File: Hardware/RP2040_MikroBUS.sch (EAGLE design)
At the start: 74 parts, among them J1 SWD, J3 Qwiic, J5 USB C, J6 microSD, Q1 20V/4.2A/52mΩ/1.4W, U2 MAX17048, U3 MCP73831, U4 W25QXX128MBIT, U5 RP2040, U6 WS2812-2020, U7 3.3V, Y2 12MHz

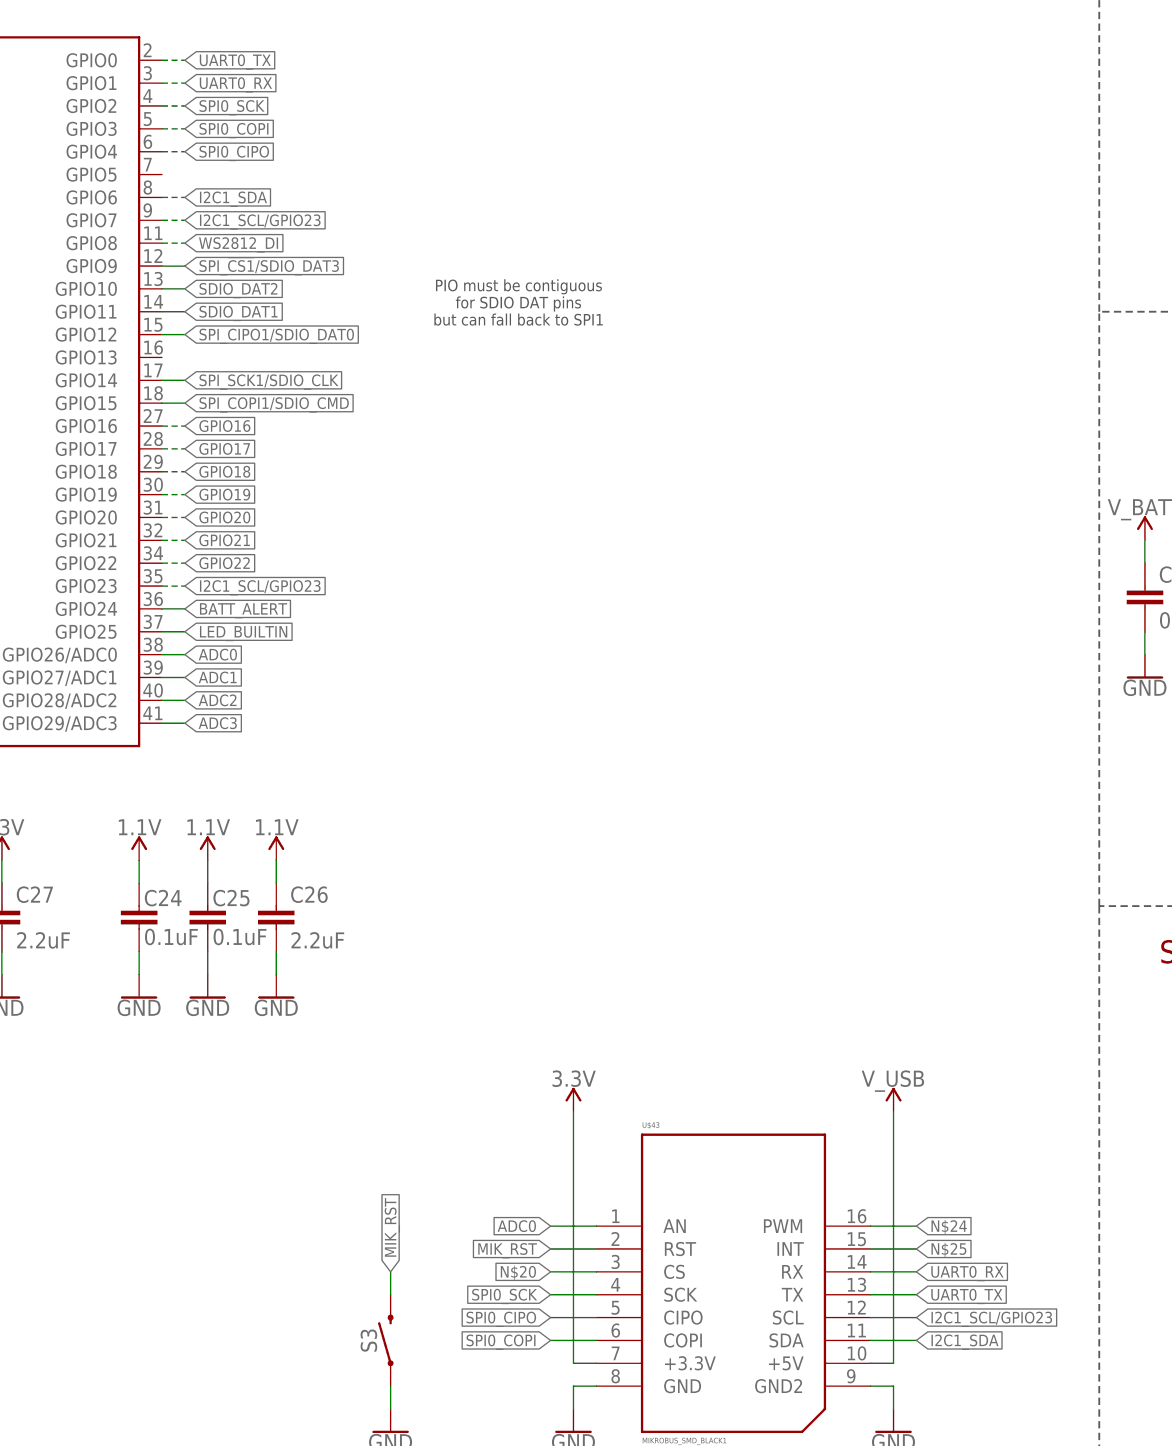
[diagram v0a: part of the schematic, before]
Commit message: Rename eagle files
Make sure everything is connected in the schematic
Parts are laid out where they should be on board, need to just route/re-route.
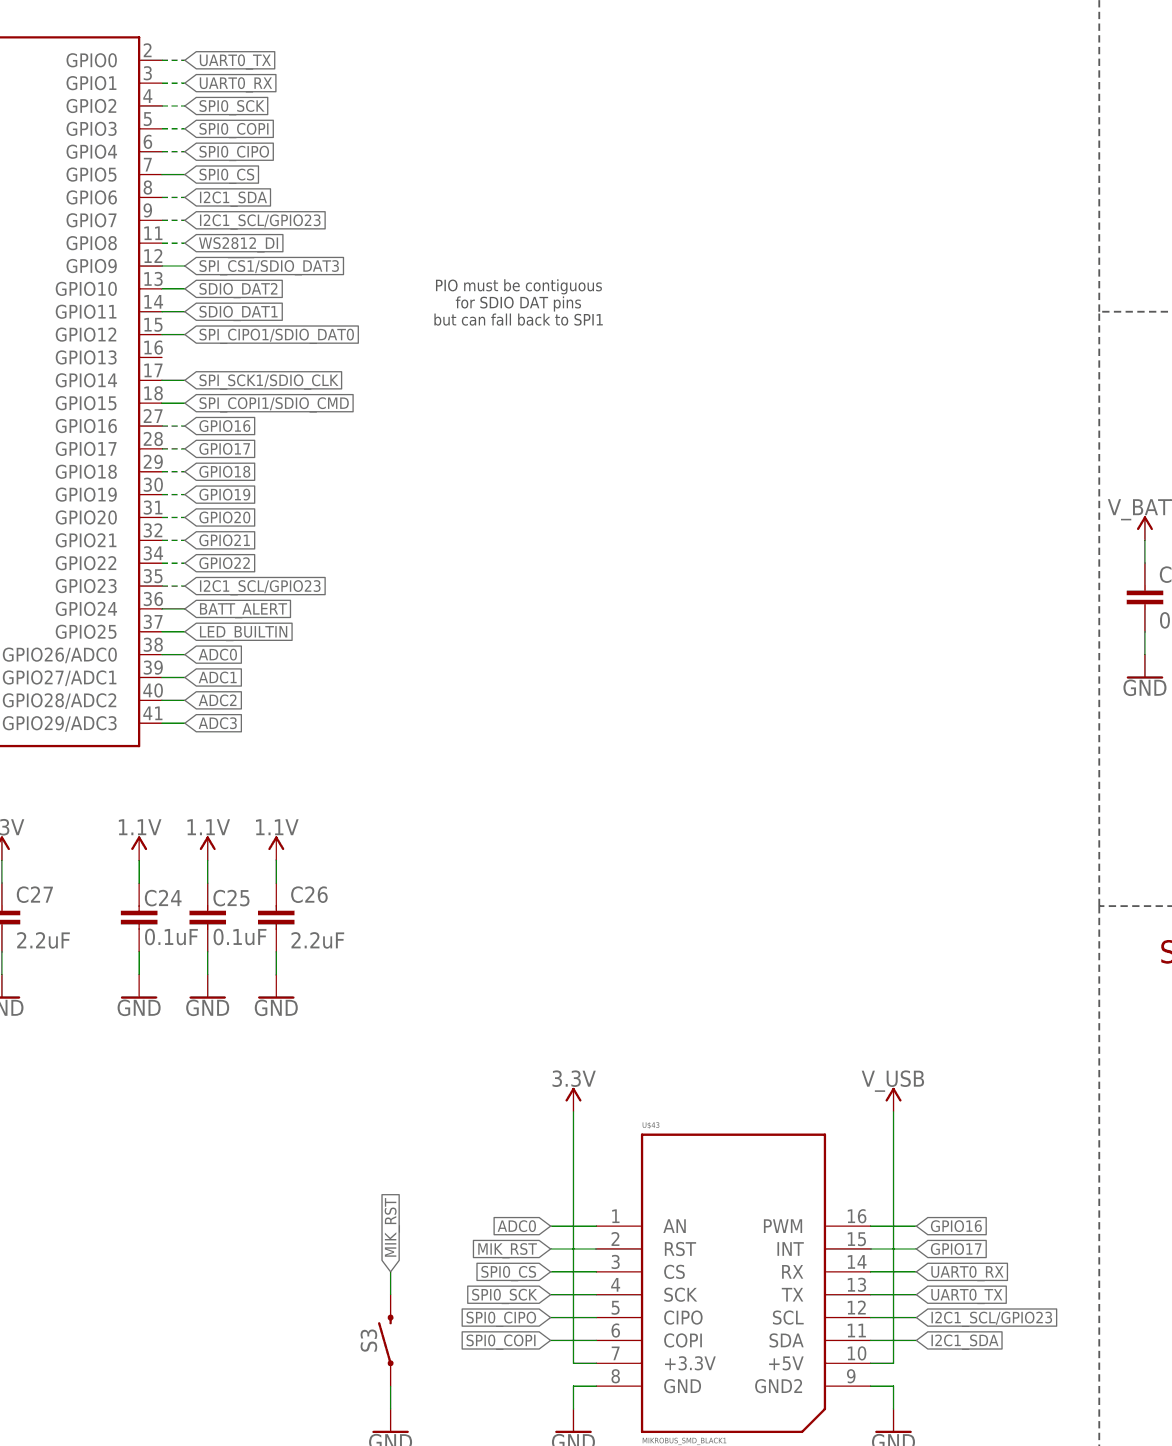
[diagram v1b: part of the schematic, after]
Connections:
- removed net N$20: U$43.CS
- removed net N$24: U$43.PWM
- removed net N$25: U$43.INT
- new net SPI0_CS: U$43.CS, U5.GPIO5
- net GPIO16: now also U$43.PWM
- net GPIO17: now also U$43.INT
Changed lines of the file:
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@@
 <?xml version="1.0" encoding="utf-8"?>
 <!DOCTYPE eagle SYSTEM "eagle.dtd">
-<eagle version="9.4.2">
+<eagle version="9.5.2">
 <drawing>
 <settings>
-<setting alwaysvectorfont="yes"/>
+<setting alwaysvectorfont="no"/>
 <setting keepoldvectorfont="yes"/>
 <setting verticaltext="up"/>
@@
 <label x="365.76" y="81.28" size="1.27" layer="95" rot="R180" xref="yes"/>
 </segment>
+<segment>
+<pinref part="U$43" gate="J1" pin="PWM"/>
+<wire x1="172.72" y1="30.48" x2="177.8" y2="30.48" width="0.1524" layer="91"/>
+<label x="177.8" y="30.48" size="1.27" layer="95" xref="yes"/>
+</segment>
 </net>
 <net name="GPIO17" class="0">
@@
 <wire x1="368.3" y1="78.74" x2="365.76" y2="78.74" width="0.1524" layer="91" style="longdash"/>
 <label x="365.76" y="78.74" size="1.27" layer="95" rot="R180" xref="yes"/>
+</segment>
+<segment>
+<pinref part="U$43" gate="J1" pin="INT"/>
+<wire x1="172.72" y1="27.94" x2="177.8" y2="27.94" width="0.1524" layer="91"/>
+<label x="177.8" y="27.94" size="1.27" layer="95" xref="yes"/>
 </segment>
 </net>
@@
 </segment>
 </net>
-<net name="N$20" class="0">
+<net name="SPI0_CS" class="0">
+<segment>
+<pinref part="U5" gate="U1" pin="GPIO5"/>
+<wire x1="93.98" y1="147.32" x2="96.52" y2="147.32" width="0.1524" layer="91"/>
+<label x="96.52" y="147.32" size="1.27" layer="95" xref="yes"/>
+</segment>
 <segment>
 <pinref part="U$43" gate="J1" pin="CS"/>
@@
 </segment>
 </net>
-<net name="N$24" class="0">
-<segment>
-<pinref part="U$43" gate="J1" pin="PWM"/>
-<wire x1="172.72" y1="30.48" x2="177.8" y2="30.48" width="0.1524" layer="91"/>
-<label x="177.8" y="30.48" size="1.27" layer="95" xref="yes"/>
-</segment>
-</net>
-<net name="N$25" class="0">
-<segment>
-<pinref part="U$43" gate="J1" pin="INT"/>
-<wire x1="172.72" y1="27.94" x2="177.8" y2="27.94" width="0.1524" layer="91"/>
-<label x="177.8" y="27.94" size="1.27" layer="95" xref="yes"/>
-</segment>
-</net>

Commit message: Routing finished!
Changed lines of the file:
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@@
 <?xml version="1.0" encoding="utf-8"?>
 <!DOCTYPE eagle SYSTEM "eagle.dtd">
-<eagle version="9.5.2">
+<eagle version="9.4.2">
 <drawing>
 <settings>
-<setting alwaysvectorfont="no"/>
+<setting alwaysvectorfont="yes"/>
 <setting keepoldvectorfont="yes"/>
 <setting verticaltext="up"/>
@@
 <layer number="56" name="wert" color="7" fill="1" visible="no" active="no"/>
 <layer number="57" name="tCAD" color="7" fill="1" visible="no" active="no"/>
+<layer number="58" name="bCopper" color="7" fill="1" visible="no" active="no"/>
 <layer number="59" name="tCarbon" color="7" fill="1" visible="no" active="no"/>
 <layer number="60" name="bCarbon" color="7" fill="1" visible="no" active="no"/>
@@
 <layer number="154" name="FabDoc2" color="7" fill="1" visible="yes" active="yes"/>
 <layer number="155" name="FabDoc3" color="7" fill="1" visible="yes" active="yes"/>
+<layer number="156" name="gesam-Maß" color="1" fill="7" visible="no" active="no"/>
+<layer number="157" name="FaceMchng" color="3" fill="1" visible="no" active="no"/>
+<layer number="158" name="FaceMMeas" color="3" fill="1" visible="no" active="no"/>
+<layer number="159" name="Geh-Bear2" color="1" fill="7" visible="no" active="no"/>
+<layer number="160" name="Topologie" color="9" fill="1" visible="no" active="no"/>
+<layer number="161" name="tomplace2" color="7" fill="1" visible="no" active="no"/>
 <layer number="166" name="AntennaArea" color="7" fill="1" visible="no" active="no"/>
 <layer number="168" name="4mmHeightArea" color="7" fill="1" visible="no" active="no"/>
@@
 <layer number="250" name="Descript" color="3" fill="1" visible="no" active="no"/>
 <layer number="251" name="SMDround" color="12" fill="11" visible="no" active="no"/>
+<layer number="252" name="BR-BS" color="7" fill="1" visible="no" active="no"/>
+<layer number="253" name="Extra" color="7" fill="1" visible="no" active="no"/>
 <layer number="254" name="cooling" color="7" fill="1" visible="yes" active="yes"/>
 <layer number="255" name="routoute" color="7" fill="1" visible="yes" active="yes"/>
@@
 <part name="SUPPLY36" library="SparkFun-PowerSymbols" deviceset="3.3V" device=""/>
 <part name="GND42" library="SparkFun-PowerSymbols" deviceset="GND" device=""/>
-<part name="TP1" library="SparkFun-Connectors" deviceset="TEST-POINT" device="3X4" value=""/>
-<part name="TP2" library="SparkFun-Connectors" deviceset="TEST-POINT" device="3X4" value=""/>
-<part name="TP3" library="SparkFun-Connectors" deviceset="TEST-POINT" device="3X4" value=""/>
+<part name="TP1" library="SparkFun-Connectors" deviceset="TEST-POINT" device="3X4" value="TEST-POINT3X4"/>
+<part name="TP2" library="SparkFun-Connectors" deviceset="TEST-POINT" device="3X4" value="TEST-POINT3X4"/>
+<part name="TP3" library="SparkFun-Connectors" deviceset="TEST-POINT" device="3X4" value="TEST-POINT3X4"/>
 <part name="U$43" library="mikroBUS_SMD_BLACK" deviceset="MIKROBUS_SMD_BLACK" device="1" package3d_urn="urn:adsk.eagle:package:18494266/4"/>
 <part name="GND43" library="SparkFun-PowerSymbols" deviceset="GND" device=""/>

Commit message: Made board dimensions on grid
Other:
- note added: "MikroBUS socket"
- note added: "v01"
- note removed: "v10"
- moved on the sheet: C17, C18, C20, C21, C22, C23, C24, C25, C26, C27

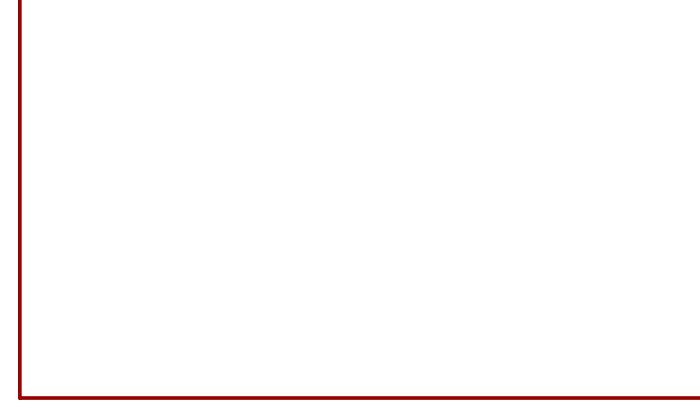
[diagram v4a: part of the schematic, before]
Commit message: More of Pete's updates
* Fix I2C jumper label
* Update RP2040 logo and add to SF Eagle libraries
* Change "Mik" to "Mikro" for mikroBUS reset button
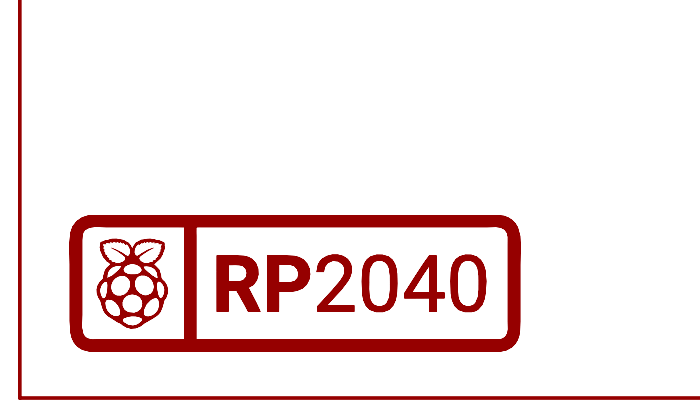
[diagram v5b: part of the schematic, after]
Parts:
- added U$17, U$73: RASPI_RP2040_LOGO_10MM, SparkFun-Aesthetics:RASPI_RP2040_LOGO_10MM
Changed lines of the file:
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@@
 <?xml version="1.0" encoding="utf-8"?>
 <!DOCTYPE eagle SYSTEM "eagle.dtd">
-<eagle version="9.5.2">
+<eagle version="9.4.2">
 <drawing>
 <settings>
-<setting alwaysvectorfont="no"/>
+<setting alwaysvectorfont="yes"/>
 <setting keepoldvectorfont="yes"/>
 <setting verticaltext="up"/>
@@
 <part name="S3" library="SparkFun-Switches" deviceset="MOMENTARY-SWITCH-SPST" device="-SMD-5.2MM-TALL"/>
 <part name="GND45" library="SparkFun-PowerSymbols" deviceset="GND" device=""/>
+<part name="U$17" library="SparkFun-Aesthetics" deviceset="RASPI_RP2040_LOGO" device="_10MM"/>
+<part name="U$73" library="SparkFun-Aesthetics" deviceset="RASPI_RP2040_LOGO" device="_10MM"/>
 </parts>
 <sheets>
@@
 <attribute name="VALUE" x="119.38" y="7.366" size="1.778" layer="96" align="top-center"/>
 </instance>
+<instance part="U$17" gate="G$1" x="30.48" y="12.7" smashed="yes"/>
+<instance part="U$73" gate="G$1" x="30.48" y="12.7" smashed="yes"/>
 </instances>
 <busses>

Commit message: Schematic updates
* Remove values from TPs
* Updated net labels with "!" for active low signals - !BOOT!, !SPI0_CS!, !QSPI-CS!, !BATT_ALERT!
* Updated name, value, and shape of mikroBUS socket sch symbol
* Switched out SD card socket for the new one, did NOT connect the detect pin
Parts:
- removed U$43: MIKROBUS_SMD_BLACK1, mikroBUS_SMD_BLACK:MIKROBUS_SMD_BLACK1
- added J9: MIKROBUS_SMD_BLACK1, mikroBUS_SMD_BLACK:MIKROBUS_SMD_BLACK1
- J6: device SparkFun-Connectors:MICRO-SD-SDIOPUSH-PUSH -> SparkFun-Connectors:MICRO-SD-PUSH-PUSH-EXT-PIN
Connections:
- net BATT_ALERT renamed !BATT_ALERT!
- net BOOT renamed !BOOT!
- net QSPI-CS renamed !QSPI-CS!
- removed net SPI0_CS: U$43.CS, U5.GPIO5
- new net !SPI0_CS!: J9.CS, U5.GPIO5
- net 3.3V: now also J9.+3.3V; no longer U$43.+3.3V
- net ADC0: now also J9.AN; no longer U$43.AN
- net GND: now also J6.DET, J9.GND, J9.GND2; no longer J6.SHIELD, U$43.GND, U$43.GND2
- net GPIO16: now also J9.PWM; no longer U$43.PWM
- net GPIO17: now also J9.INT; no longer U$43.INT
- net I2C1_SCL/GPIO23: now also J9.SCL; no longer U$43.SCL
- net I2C1_SDA: now also J9.SDA; no longer U$43.SDA
- net MIK_RST: now also J9.RST; no longer U$43.RST
- net SDIO_DAT1: now also J6.DAT1; no longer J6.DAT1/NC
- net SDIO_DAT2: now also J6.DAT2; no longer J6.DAT2/NC
- net SPI0_CIPO: now also J9.CIPO; no longer U$43.CIPO
- net SPI0_COPI: now also J9.COPI; no longer U$43.COPI
- net SPI0_SCK: now also J9.SCK; no longer U$43.SCK
- net UART0_RX: now also J9.RX; no longer U$43.RX
- net UART0_TX: now also J9.TX; no longer U$43.TX
- net V_USB: now also J9.+5V; no longer U$43.+5V
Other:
- moved on the sheet: S3
